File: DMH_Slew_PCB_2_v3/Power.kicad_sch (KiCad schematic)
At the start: 29 parts, among them J0 Conn_01x01, J100 IDC_02x08, J200 IDC_02x05, J50 Conn_01x08_PinHeader, J51 Conn_01x08_PinHeader, J60 Conn_01x08_PinHeader, J61 Conn_01x08_PinHeader, U1 TL074, U10 LM4040LP-10, U11 LM4040LP-10, U2 TL074, U3 TL074, U4 TL074

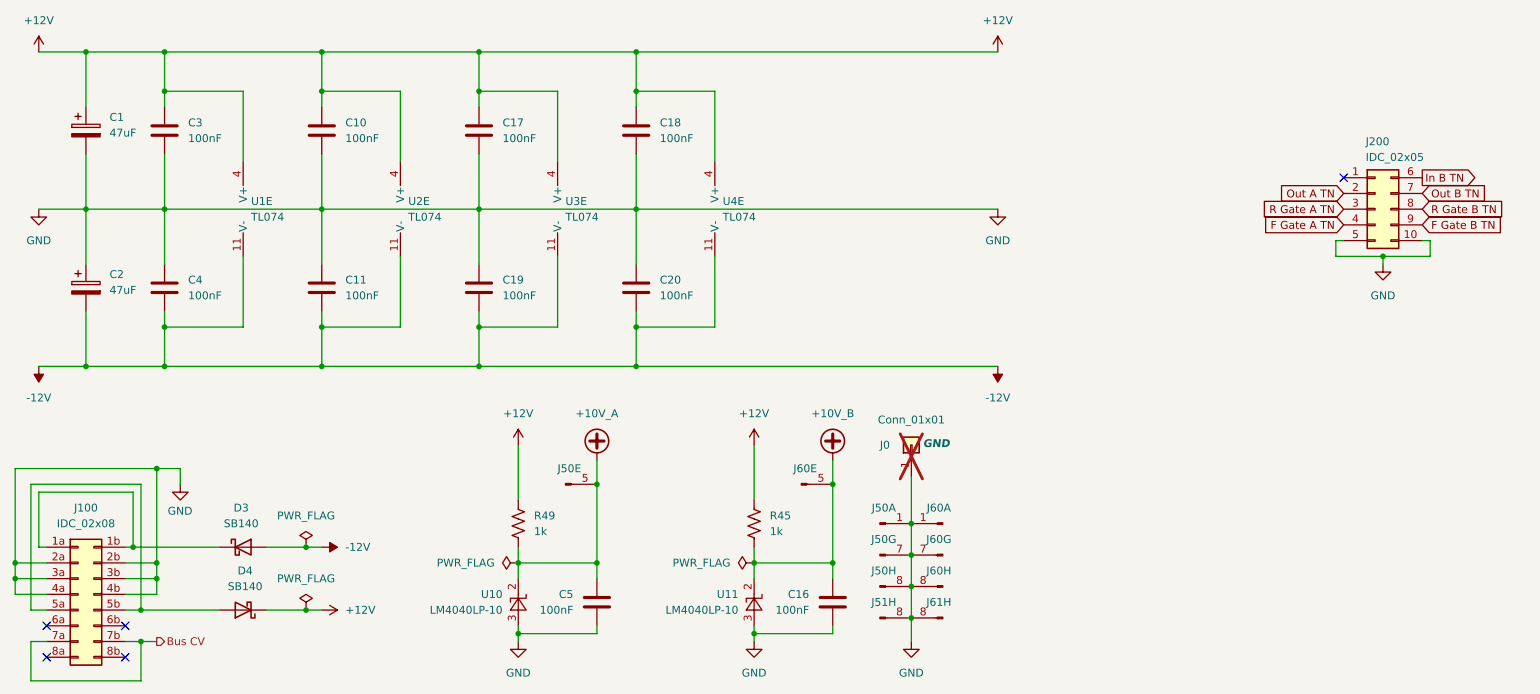
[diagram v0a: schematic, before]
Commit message: Relinked PCB1 and 2 with new v3 schematics
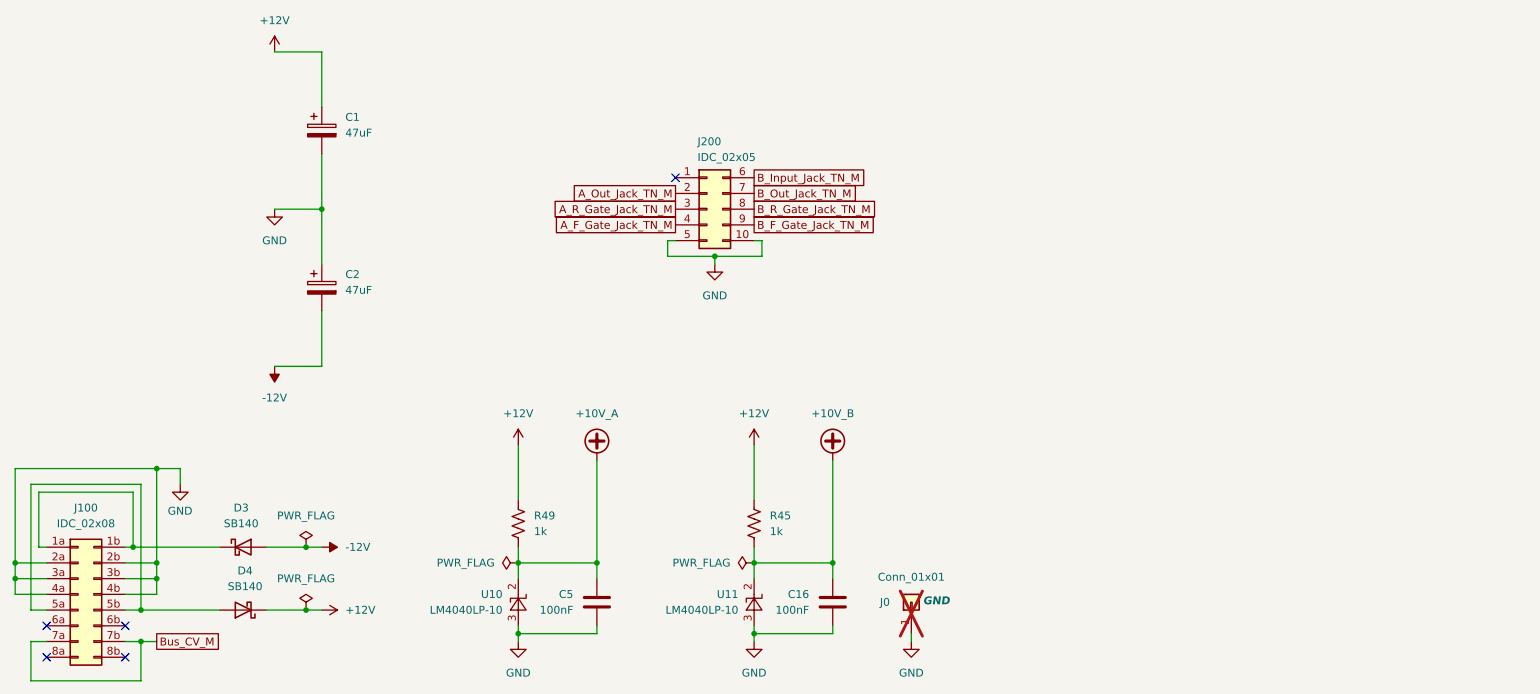
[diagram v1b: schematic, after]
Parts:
- removed C10, C11, C17, C18, C19, C20, C3, C4: 100nF, Capacitor_THT:C_Disc_D4.3mm_W1.9mm_P5.00mm, symbol Device:C
- removed J50, J51, J60, J61: Conn_01x08_PinHeader, Connector_PinSocket_2.54mm:PinSocket_1x08_P2.54mm_Vertical, symbol SynthStuff:Conn_01x08_PinHeader
- removed U1, U3: TL074, Package_DIP:DIP-16_W7.62mm_Socket, symbol Amplifier_Operational:TL074
- removed U2, U4: TL074, Package_DIP:DIP-14_W7.62mm_Socket, symbol Amplifier_Operational:TL074
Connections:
- net Bus CV renamed Bus_CV_M
- net F Gate A TN renamed A_F_Gate_Jack_TN_M
- net F Gate B TN renamed B_F_Gate_Jack_TN_M
- net In B TN renamed B_Input_Jack_TN_M
- net Out A TN renamed A_Out_Jack_TN_M
- net Out B TN renamed B_Out_Jack_TN_M
- net R Gate A TN renamed A_R_Gate_Jack_TN_M
- net R Gate B TN renamed B_R_Gate_Jack_TN_M
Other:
- moved on the sheet: C1, C2, J0, J200

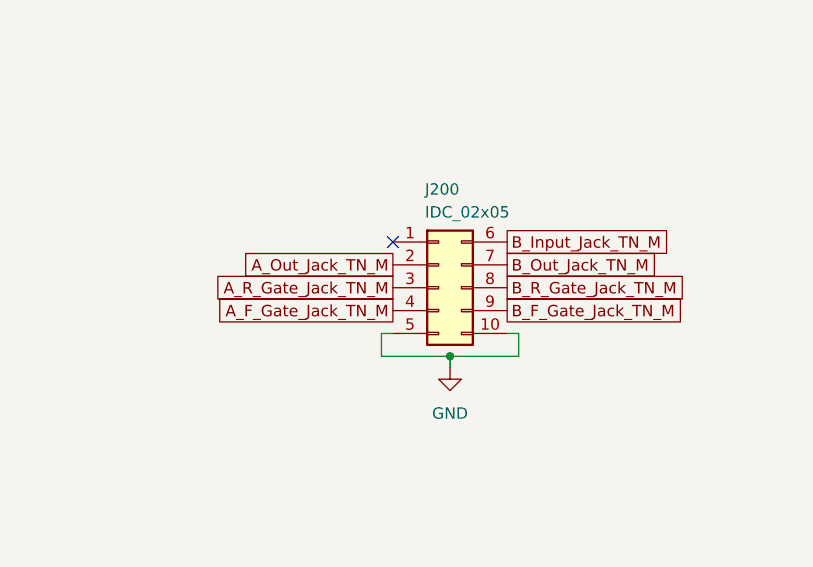
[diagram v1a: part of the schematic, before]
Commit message: Exposed loopback resistor to submodule connector
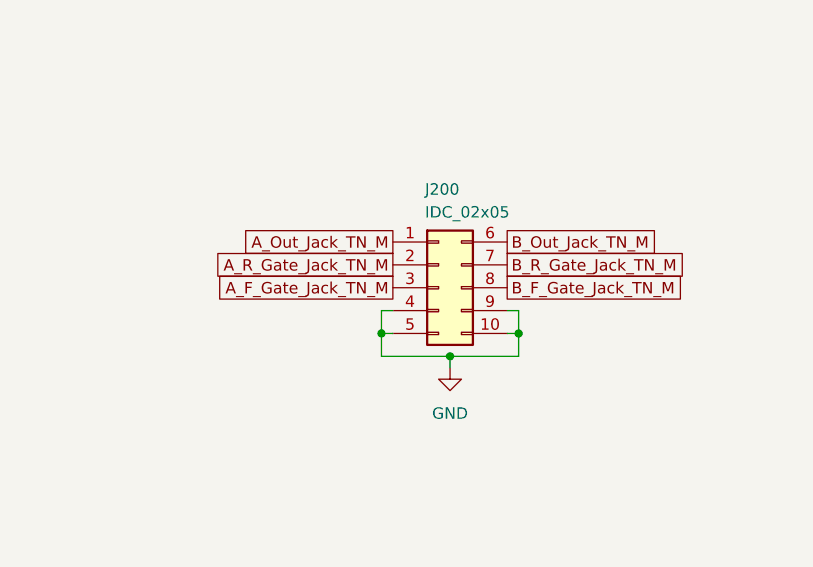
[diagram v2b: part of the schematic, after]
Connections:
- net B_Input_Jack_TN_M is gone; now on net B_Out_Jack_TN_M: J200.6 (Pin_6)
- net A_F_Gate_Jack_TN_M: now also J200.3 (Pin_3); no longer J200.4 (Pin_4)
- net A_Out_Jack_TN_M: now also J200.1 (Pin_1); no longer J200.2 (Pin_2)
- net A_R_Gate_Jack_TN_M: now also J200.2 (Pin_2); no longer J200.3 (Pin_3)
- net B_F_Gate_Jack_TN_M: now also J200.8 (Pin_8); no longer J200.9 (Pin_9)
- net B_Out_Jack_TN_M: no longer J200.7 (Pin_7)
- net B_R_Gate_Jack_TN_M: now also J200.7 (Pin_7); no longer J200.8 (Pin_8)
- net GND: now also J200.4 (Pin_4), J200.9 (Pin_9)
- no-connect marks 5 -> 4
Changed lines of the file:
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@@
+	)
+	(junction
+		(at 134.62 125.73)
+		(diameter 0)
+		(color 0 0 0 0)
 	)
 	(junction
 		(at 63.5 120.65)
+		(diameter 0)
+		(color 0 0 0 0)
+	)
+	(junction
+		(at 119.38 125.73)
 		(diameter 0)
 		(color 0 0 0 0)
@@
 	)
 	(no_connect
-		(at 120.65 115.57)
-	)
-	(no_connect
 		(at 19.05 187.96)
 	)
@@
 	(wire
 		(pts
+			(xy 119.38 123.19) (xy 119.38 125.73)
+		)
+		(stroke
+			(width 0)
+			(type default)
+		)
+	)
+	(wire
+		(pts
 			(xy 34.29 165.1) (xy 34.29 185.42)
 		)
@@
 	(wire
 		(pts
+			(xy 134.62 123.19) (xy 134.62 125.73)
+		)
+		(stroke
+			(width 0)
+			(type default)
+		)
+	)
+	(wire
+		(pts
 			(xy 133.35 189.23) (xy 133.35 190.5)
 		)
@@
 	(wire
 		(pts
+			(xy 133.35 123.19) (xy 134.62 123.19)
+		)
+		(stroke
+			(width 0)
+			(type default)
+		)
+	)
+	(wire
+		(pts
+			(xy 120.65 123.19) (xy 119.38 123.19)
+		)
+		(stroke
+			(width 0)
+			(type default)
+		)
+	)
+	(wire
+		(pts
 			(xy 134.62 125.73) (xy 134.62 128.27)
 		)
@@
 		)
 	)
-	(global_label "B_Out_Jack_TN_M"
+	(global_label "A_R_Gate_Jack_TN_M"
 		(shape passive)
-		(at 133.35 118.11 0)
+		(at 120.65 118.11 180)
 		(fields_autoplaced yes)
 		(effects
@@
 				(size 1.27 1.27)
 			)
+			(justify right)
+		)
+		(property "Intersheetrefs" "${INTERSHEET_REFS}"
+			(at 98.2521 118.11 0)
+			(effects
+				(font
+					(size 1.27 1.27)
+				)
+				(justify right)
+				(hide yes)
+			)
+		)
+	)
+	(global_label "B_F_Gate_Jack_TN_M"
+		(shape passive)
+		(at 133.35 120.65 0)
+		(fields_autoplaced yes)
+		(effects
+			(font
+				(size 1.27 1.27)
+			)
 			(justify left)
 		)
 		(property "Intersheetrefs" "${INTERSHEET_REFS}"
-			(at 152.6636 118.11 0)
+			(at 155.7479 120.65 0)
 			(effects
 				(font
@@
 		)
 	)
-	(global_label "A_Out_Jack_TN_M"
+	(global_label "A_F_Gate_Jack_TN_M"
 		(shape passive)
-		(at 120.65 118.11 180)
+		(at 120.65 120.65 180)
 		(fields_autoplaced yes)
 		(effects
@@
 		)
 		(property "Intersheetrefs" "${INTERSHEET_REFS}"
-			(at 101.5178 118.11 0)
+			(at 98.4335 120.65 0)
 			(effects
 				(font
@@
 				)
 				(justify right)
-				(hide yes)
-			)
-		)
-	)
-	(global_label "B_F_Gate_Jack_TN_M"
-		(shape passive)
-		(at 133.35 123.19 0)
-		(fields_autoplaced yes)
-		(effects
-			(font
-				(size 1.27 1.27)
-			)
-			(justify left)
-		)
-		(property "Intersheetrefs" "${INTERSHEET_REFS}"
-			(at 155.7479 123.19 0)
-			(effects
-				(font
-					(size 1.27 1.27)
-				)
-				(justify left)
-				(hide yes)
-			)
-		)
-	)
-	(global_label "B_R_Gate_Jack_TN_M"
-		(shape passive)
-		(at 133.35 120.65 0)
-		(fields_autoplaced yes)
-		(effects
-			(font
-				(size 1.27 1.27)
-			)
-			(justify left)
-		)
-		(property "Intersheetrefs" "${INTERSHEET_REFS}"
-			(at 155.9293 120.65 0)
-			(effects
-				(font
-					(size 1.27 1.27)
-				)
-				(justify left)
-				(hide yes)
-			)
-		)
-	)
-	(global_label "B_Input_Jack_TN_M"
-		(shape passive)
-		(at 133.35 115.57 0)
-		(fields_autoplaced yes)
-		(effects
-			(font
-				(size 1.27 1.27)
-			)
-			(justify left)
-		)
-		(property "Intersheetrefs" "${INTERSHEET_REFS}"
-			(at 154.2359 115.57 0)
-			(effects
-				(font
-					(size 1.27 1.27)
-				)
-				(justify left)
 				(hide yes)
 			)
@@
 		)
 	)
-	(global_label "A_F_Gate_Jack_TN_M"
+	(global_label "A_Out_Jack_TN_M"
 		(shape passive)
-		(at 120.65 123.19 180)
+		(at 120.65 115.57 180)
 		(fields_autoplaced yes)
 		(effects
@@
 		)
 		(property "Intersheetrefs" "${INTERSHEET_REFS}"
-			(at 98.4335 123.19 0)
+			(at 101.5178 115.57 0)
 			(effects
 				(font
@@
 		)
 	)
-	(global_label "A_R_Gate_Jack_TN_M"
+	(global_label "B_R_Gate_Jack_TN_M"
 		(shape passive)
-		(at 120.65 120.65 180)
+		(at 133.35 118.11 0)
 		(fields_autoplaced yes)
 		(effects
@@
 				(size 1.27 1.27)
 			)
-			(justify right)
+			(justify left)
 		)
 		(property "Intersheetrefs" "${INTERSHEET_REFS}"
-			(at 98.2521 120.65 0)
+			(at 155.9293 118.11 0)
 			(effects
 				(font
 					(size 1.27 1.27)
 				)
-				(justify right)
+				(justify left)
 				(hide yes)
 			)
+		)
+	)
+	(global_label "B_Out_Jack_TN_M"
+		(shape passive)
+		(at 133.35 115.57 0)
+		(fields_autoplaced yes)
+		(effects
+			(font
+				(size 1.27 1.27)
+			)
+			(justify left)
+		)
+		(property "Intersheetrefs" "${INTERSHEET_REFS}"
+			(at 152.6636 115.57 0)
+			(effects
+				(font
+					(size 1.27 1.27)
+				)
+				(justify left)
+				(hide yes)
+			)

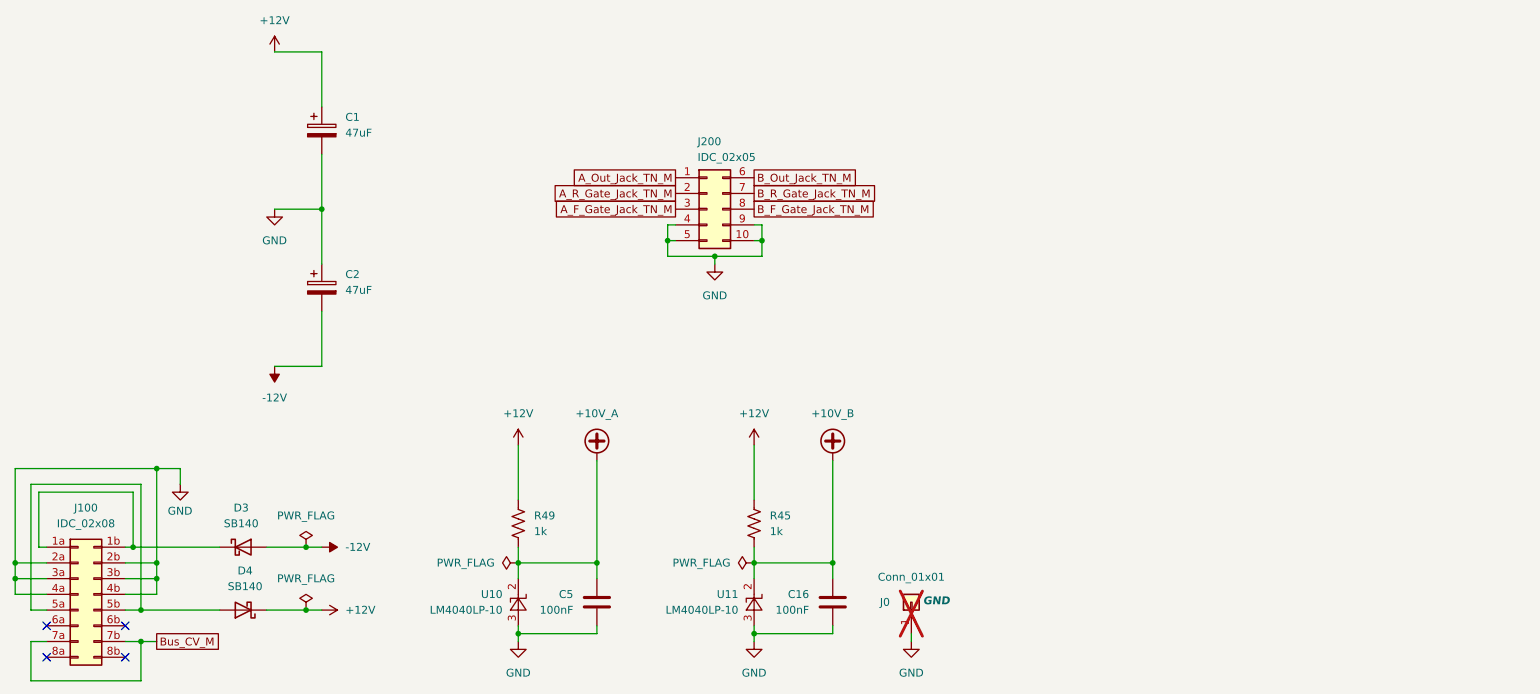
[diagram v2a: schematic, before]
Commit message: Redesigned Main PCB
and regenerated Gerbers
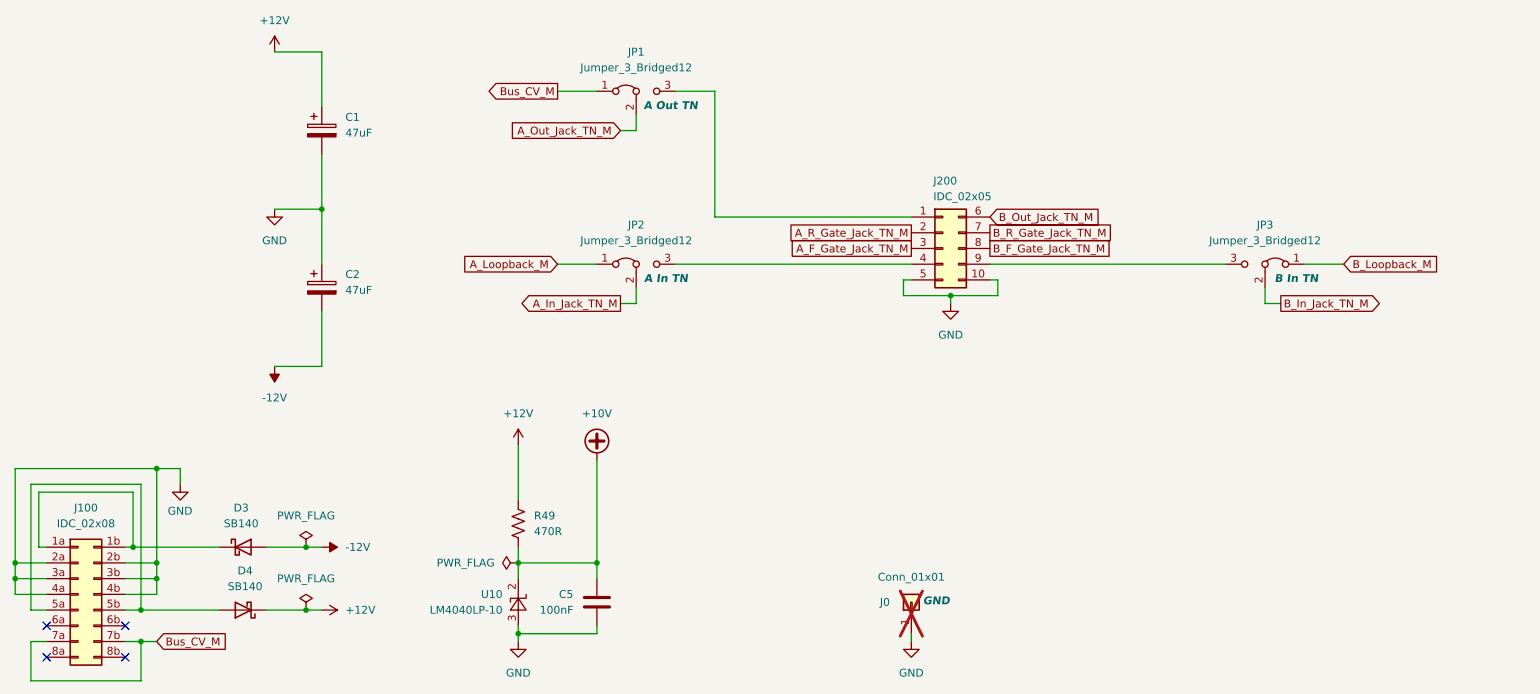
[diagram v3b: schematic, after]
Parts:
- removed C16: 100nF, Capacitor_THT:C_Disc_D4.3mm_W1.9mm_P5.00mm, symbol Device:C
- removed R45: 1k, Resistor_THT:R_Axial_DIN0207_L6.3mm_D2.5mm_P7.62mm_Horizontal, symbol Device:R_US
- removed U11: LM4040LP-10, Package_TO_SOT_THT:TO-92_Inline, symbol Reference_Voltage:LM4040LP-10
- added JP1, JP2, JP3: Jumper_3_Bridged12, Connector_PinHeader_2.54mm:PinHeader_1x03_P2.54mm_Vertical, symbol Jumper:Jumper_3_Bridged12
- R49: value 1k -> 470R
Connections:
- net A_Out_Jack_TN_M: now also JP1.2 (C); no longer J200.1 (Pin_1)
- net Bus_CV_M: now also JP1.1 (A)
- net GND: no longer J200.4 (Pin_4), J200.9 (Pin_9)
- net +10V_A renamed +10V
- new net: J200.1 (Pin_1), JP1.3 (B)
- new net: J200.4 (Pin_4), JP2.3 (B)
- new net: J200.9 (Pin_9), JP3.3 (B)
- new net A_In_Jack_TN_M: JP2.2 (C)
- new net A_Loopback_M: JP2.1 (A)
- new net B_In_Jack_TN_M: JP3.2 (C)
- new net B_Loopback_M: JP3.1 (A)
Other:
- moved on the sheet: J200
